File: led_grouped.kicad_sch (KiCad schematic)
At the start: 8 parts

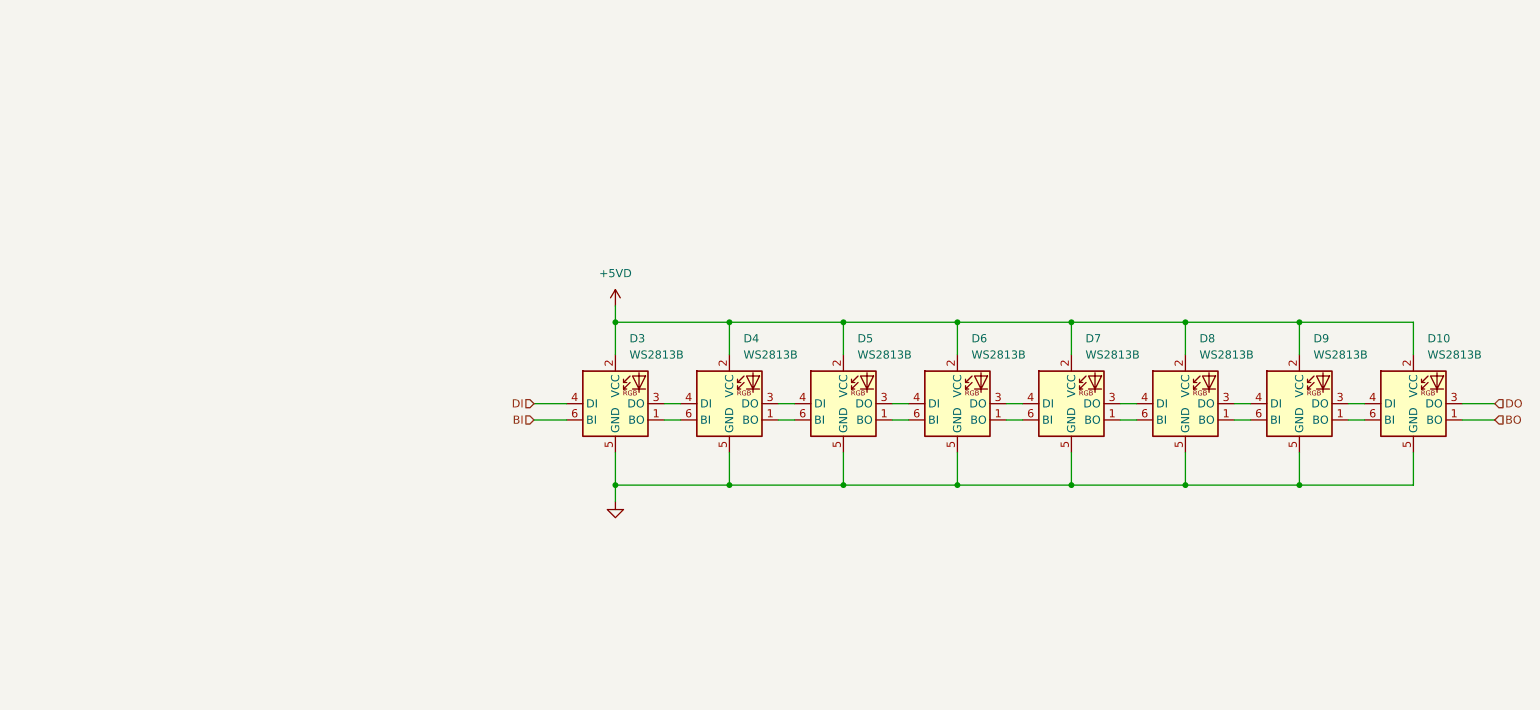
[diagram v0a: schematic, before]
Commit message: Add RGB LED schematics
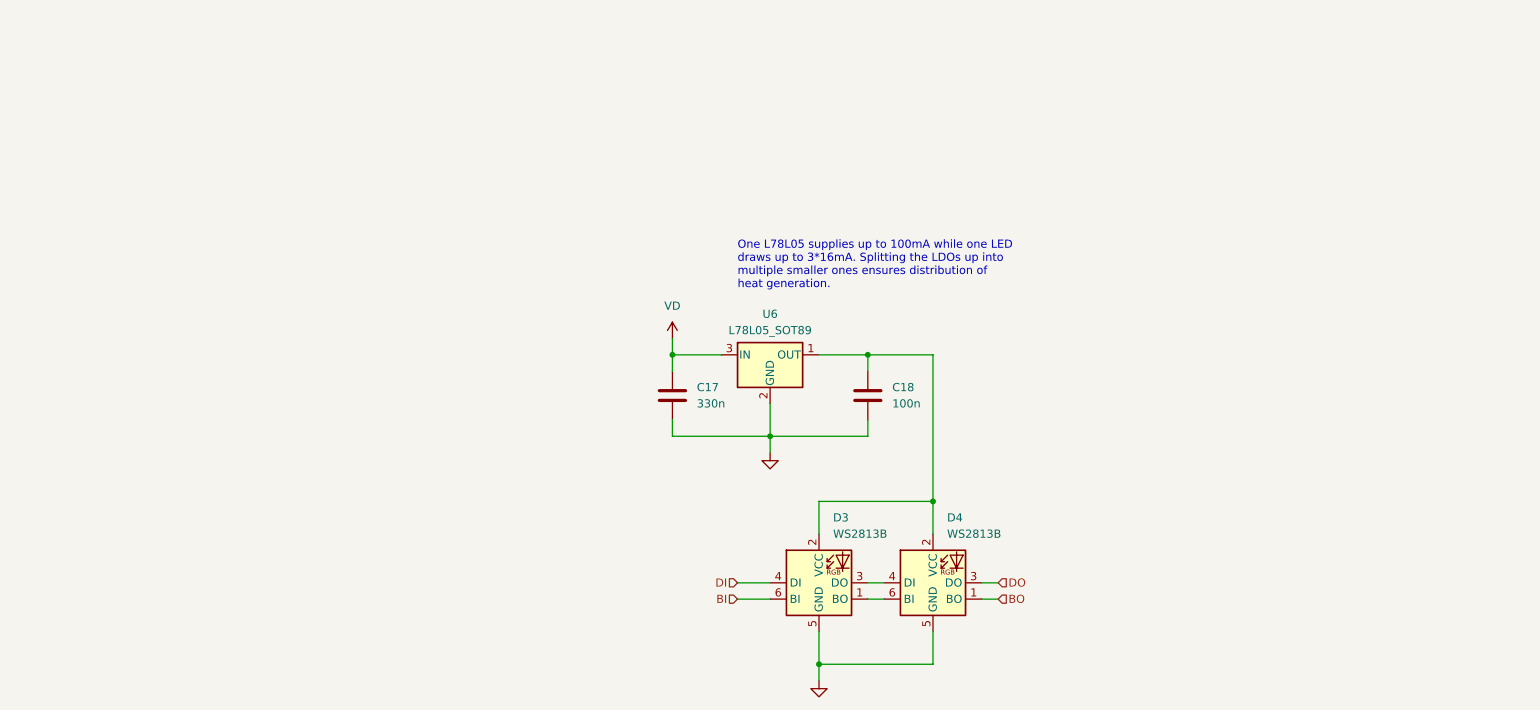
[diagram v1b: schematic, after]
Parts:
- removed D10, D5, D6, D7, D8, D9: WS2813B, symbol frodo_fancyfins:WS2813B
- added C17: 330n, symbol Device:C
- added C18: 100n, symbol Device:C
- added U6: L78L05_SOT89, Package_TO_SOT_SMD:SOT-89-3, symbol Regulator_Linear:L78L05_SOT89
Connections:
- net BO: now also D4.1 (BO)
- net DO: now also D4.3 (DO)
- net GND: now also C17.2, C18.2, U6.2 (GND)
- net +5VD: no longer names the net of D3.2 (VCC), D4.2 (VCC)
- net +5VD: now also C18.1, U6.1 (OUT)
- new net VD: C17.1, U6.3 (IN)
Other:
- note added: "One L78L05 supplies up to 100mA while one LED draws up to 3*16mA. Splitting the LDOs up into multiple smaller ones ensures distribution of heat generation."
- moved on the sheet: D3, D4

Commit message: Schematics cleanup
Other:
- note added: "LED - power supply combination"
- moved on the sheet: C17, C18, D3, D4, U6

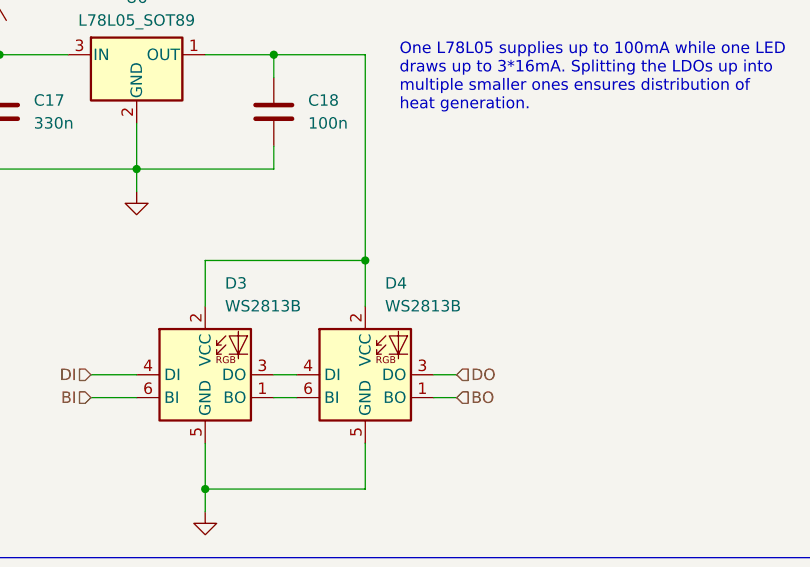
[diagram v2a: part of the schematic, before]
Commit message: Asign footprints, add missing footprints, adjust Rext.
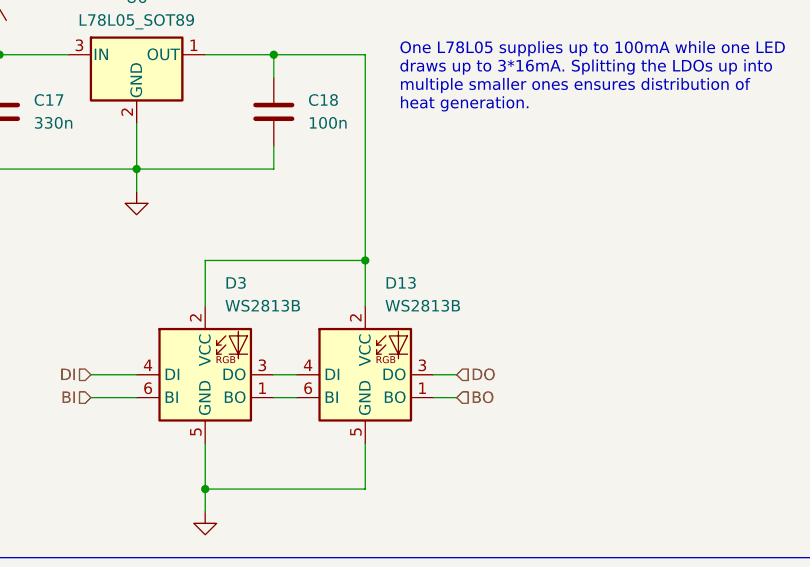
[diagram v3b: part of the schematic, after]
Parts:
- removed D4: WS2813B, symbol frodo_fancyfins:WS2813B
- added D13: WS2813B, LED_SMD:LED_WS2812_PLCC6_5.0x5.0mm_P1.6mm, symbol frodo_fancyfins:WS2813B
- C17: footprint (none) -> Capacitor_SMD:C_0603_1608Metric_Pad1.08x0.95mm_HandSolder
- C18: footprint (none) -> Capacitor_SMD:C_0402_1005Metric_Pad0.74x0.62mm_HandSolder
- D3: footprint (none) -> LED_SMD:LED_WS2812_PLCC6_5.0x5.0mm_P1.6mm
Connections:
- net BO: now also D13.1 (BO)
- net DO: now also D13.3 (DO)
- net GND: now also D13.5 (GND)
- net at C18.1, D3.2 (VCC), U6.1 (OUT): now also D13.2 (VCC)
- net at D3.1 (BO): now also D13.6 (BI)
- net at D3.3 (DO): now also D13.4 (DI)

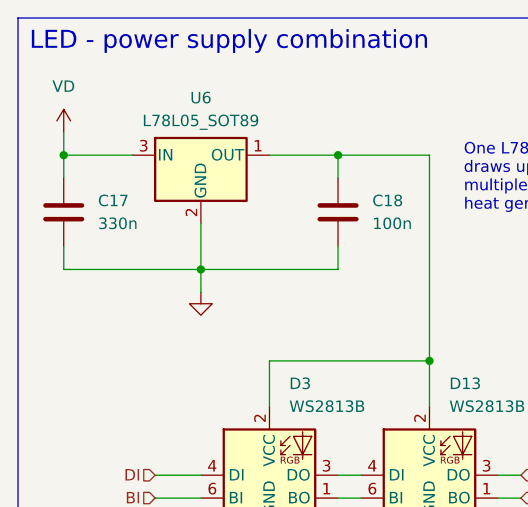
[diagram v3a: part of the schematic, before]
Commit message: add LCSC part numbers, tweak some footprints
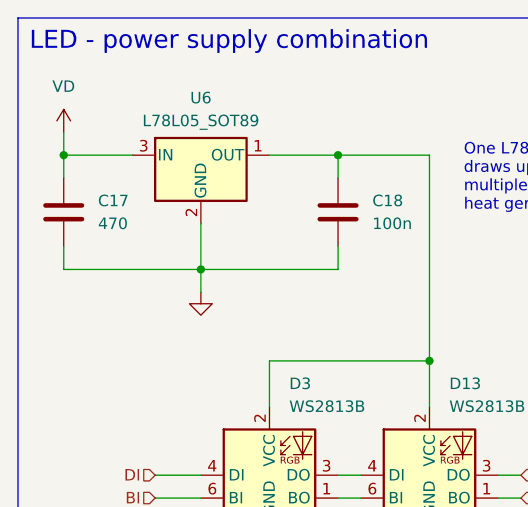
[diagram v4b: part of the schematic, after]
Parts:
- C17: value 330n -> 470; LCSC# (none) -> C1623
- C18: LCSC# (none) -> C307331
- D13, D3: LCSC# (none) -> C965558; Manufacturer (none) -> Worldsemi
- U6: LCSC# (none) -> C42738; Manufacturer (none) -> STMicroelectronics
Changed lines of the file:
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@@
+      (effects (font (size 1.27 1.27)) hide)
+    )
+    (property "LCSC#" "C307331" (at 49.53 35.56 0)
       (effects (font (size 1.27 1.27)) hide)
     )
@@
       (effects (font (size 1.27 1.27)) hide)
     )
+    (property "LCSC#" "C965558" (at 41.91 64.77 0)
+      (effects (font (size 1.27 1.27)) hide)
+    )
+    (property "Manufacturer" "Worldsemi" (at 41.91 64.77 0)
+      (effects (font (size 1.27 1.27)) hide)
+    )
     (pin "4")
     (pin "2")
@@
       (effects (font (size 1.27 1.27)) (justify left))
     )
-    (property "Value" "330n" (at 22.86 36.83 0)
+    (property "Value" "470" (at 22.86 36.83 0)
       (effects (font (size 1.27 1.27)) (justify left))
     )
@@
       (effects (font (size 1.27 1.27)) hide)
     )
+    (property "LCSC#" "C1623" (at 19.05 35.56 0)
+      (effects (font (size 1.27 1.27)) hide)
+    )
+    (property "Manufacturer" "" (at 19.05 35.56 0)
+      (effects (font (size 1.27 1.27)) hide)
+    )
     (pin "2")
     (pin "1")
@@
     )
     (property "Datasheet" "" (at 59.69 64.77 0)
+      (effects (font (size 1.27 1.27)) hide)
+    )
+    (property "LCSC#" "C965558" (at 59.69 64.77 0)
+      (effects (font (size 1.27 1.27)) hide)
+    )
+    (property "Manufacturer" "Worldsemi" (at 59.69 64.77 0)
       (effects (font (size 1.27 1.27)) hide)
     )
@@
       (effects (font (size 1.27 1.27)) hide)
     )
+    (property "LCSC#" "C42738" (at 34.29 29.21 0)
+      (effects (font (size 1.27 1.27)) hide)
+    )
+    (property "Manufacturer" "STMicroelectronics" (at 34.29 29.21 0)
+      (effects (font (size 1.27 1.27)) hide)
+    )
